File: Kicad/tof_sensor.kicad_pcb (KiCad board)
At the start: 2 copper layers, 86.4 x 45.7 mm, 57 parts, among them J1 Conn_01x06_Male, J2 Conn_01x05, Q1 Q_NMOS_SGD, SW1 SW_DIP_x03, U1 MIC5504-2.8YM5, U2 PIC24FJ64GA002, U3 VL53L0X, U4 VL53L0X, U5 PCA9306

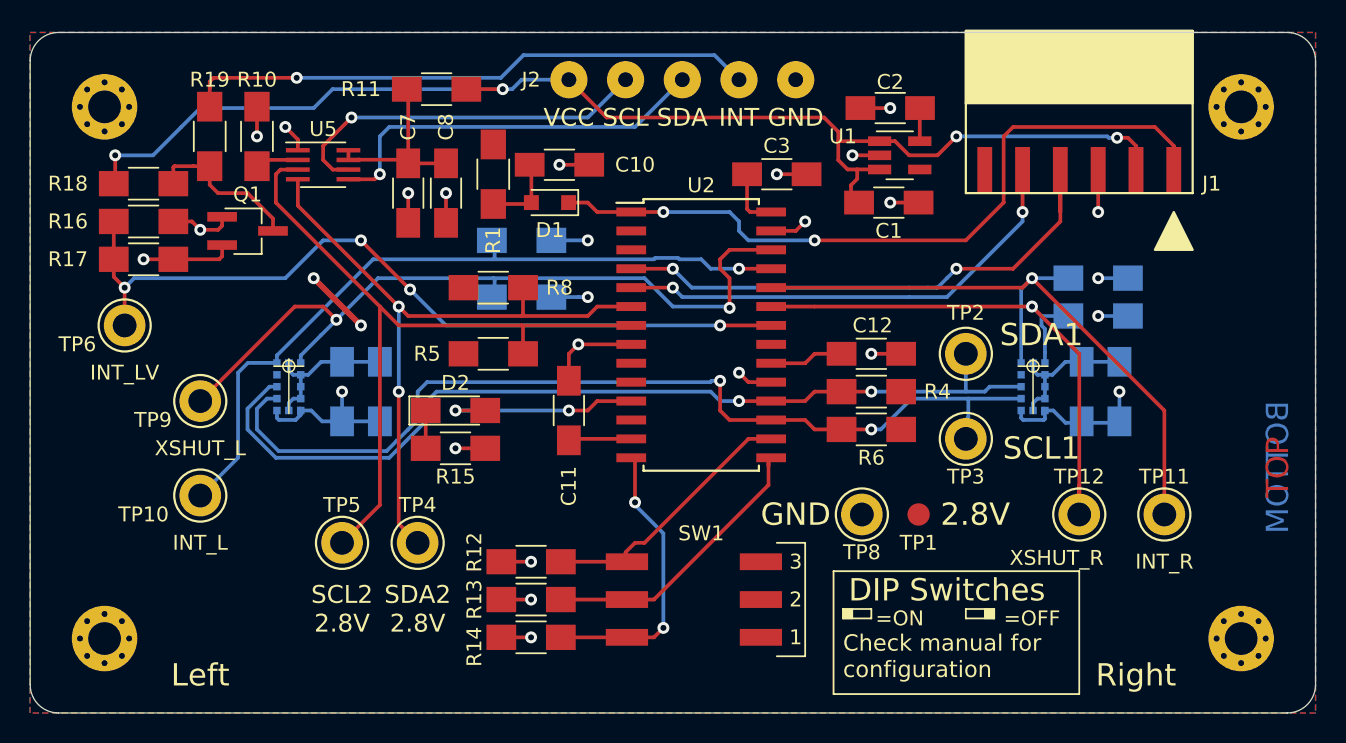
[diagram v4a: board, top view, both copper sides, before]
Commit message: Updated board files for connector pinout
Updated connector pinout so that reversing the connector would not create bad reverse polarity connection on the power supply of the board
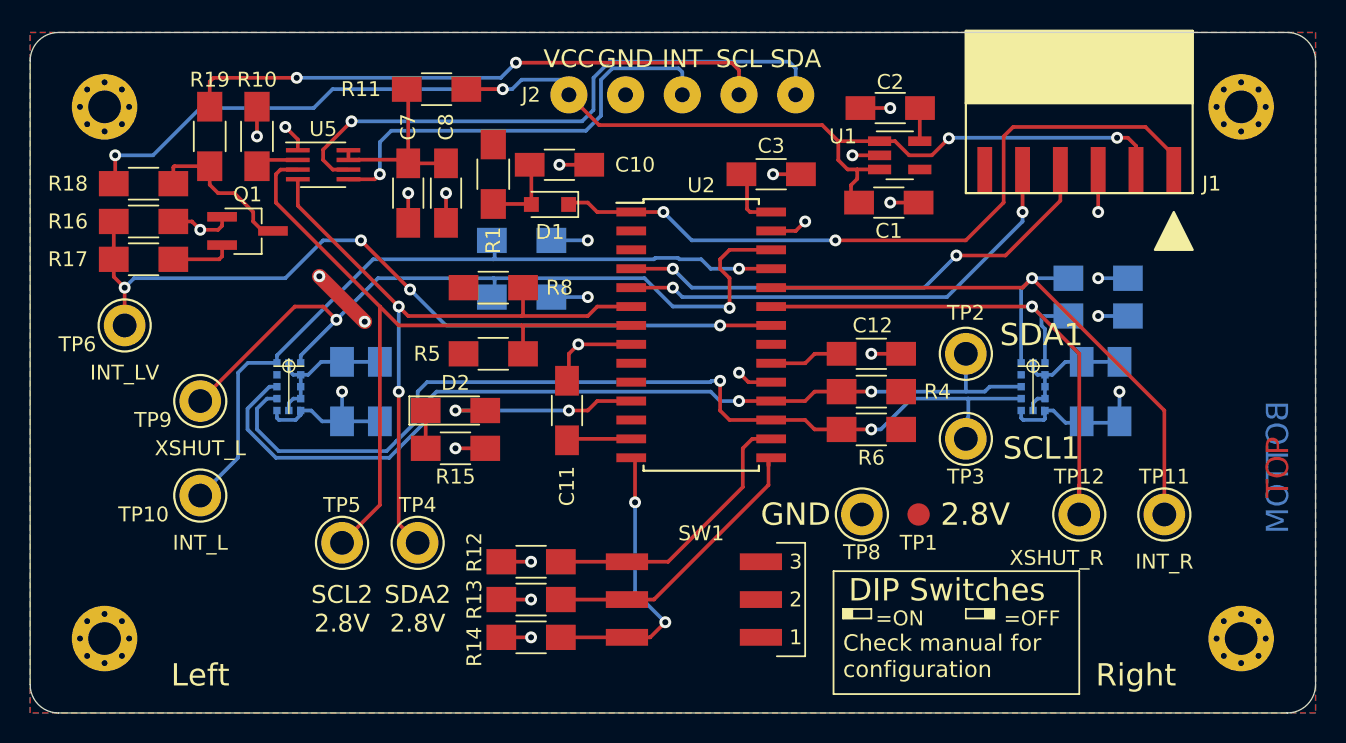
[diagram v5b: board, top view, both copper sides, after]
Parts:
- moved J2 1.02 mm to (154.9, 65.2)
- moved C3 0.38 mm to (160.9, 70.5)
- moved D1 0.13 mm to (146.1, 72.5)
- moved C11 0.13 mm to (147.2, 86.4)
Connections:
- J2 pad 2: /SCL2_HV -> GND
- J2 pad 5: GND -> /SCL2_HV
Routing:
- net /SCL2_HV: track 25.1 -> 42.0 mm
- net /ICSPDAT: track 36.7 -> 33.4 mm
- net /SDA2_HV: track 26.7 -> 29.8 mm
- net Net-(Q1-Pad2): track 6.12 -> 4.12 mm, vias 1 -> 0
- net /INT_OUT_VCC: track 38.7 -> 39.6 mm, vias 1 -> 2
- net VCC: track 86.4 -> 85.5 mm
- net /Vpp: track 49.7 -> 49.0 mm
- net /DIP3: track 18.2 -> 18.9 mm
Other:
- board text added: "12/2020"
- board text added: "V1.2"
- board text removed: "03/2020"
- board text removed: "V1.1"

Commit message: Switched to electrohype library
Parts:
- J1: footprint footprints:Conn_01x06_2.54mm_Horizontal_SMD_Handsoldered -> Electrohype_Conn:Conn_01x06_2.54mm_Horizontal_SMD_Handsoldered
- J2: footprint footprints:SolderWirePad_01x05_2-5mmDrill_HandSoldering -> Electrohype_Conn:SolderWirePad_01x05_2-5mmDrill_HandSoldering
- SW1: footprint footprints:DIP_Switch_CTS_219_Series_Gull_Wing_HandSoldered -> Electrohype_Misc:DIP_Switch_CTS_219_Series_Gull_Wing_HandSoldered
- U3, U4: footprint footprints:VL53L0X -> Electrohype_Misc:VL53L0X
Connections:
- J1 pad 6: Net-(J1-Pad6) -> (no net)
- U1 pad 4: Net-(U1-Pad4) -> (no net)
- U2 pad 10: Net-(U2-Pad10) -> (no net)
- U2 pad 12: Net-(U2-Pad12) -> (no net)
- U2 pad 2: Net-(U2-Pad2) -> (no net)
- U2 pad 21: Net-(U2-Pad21) -> (no net)
- U2 pad 3: Net-(U2-Pad3) -> (no net)
- U2 pad 9: Net-(U2-Pad9) -> (no net)
- U3 pad 8: Net-(U3-Pad8) -> (no net)
- U4 pad 8: Net-(U4-Pad8) -> (no net)
